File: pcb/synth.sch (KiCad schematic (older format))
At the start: 62 parts, among them J1 Conn_01x06, J2 Barrel_Jack_Switch, SW1 SW_Push, SW10 SW_Push, SW11 SW_Push, SW12 SW_Push, SW13 SW_Push, SW14 SW_Push, SW15 SW_Push, SW16 SW_Push, SW17 SW_Push, SW18 SW_Push, SW19 SW_Push, SW2 SW_Push, SW20 SW_Push, SW21 SW_Push, SW22 SW_Push, SW23 SW_Push, SW24 SW_Push, SW25 SW_Push, SW26 SW_Push, SW27 SW_Push, SW28 SW_Push, SW29 SW_Push, SW3 SW_Push, SW30 SW_Push, SW4 SW_Push, SW5 SW_Push, SW6 SW_Push, SW7 SW_Push, SW8 SW_Push, SW9 SW_Push, U1 LD1117S33TR_SOT223, U2 STM32F407VGTx, Y1 Crystal_8

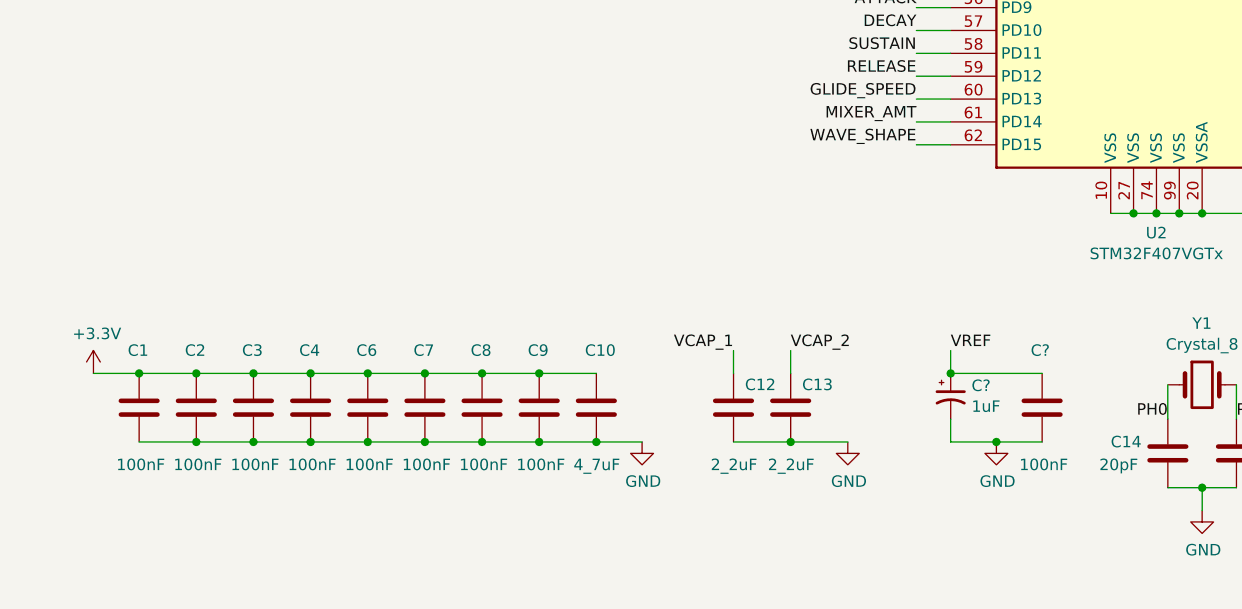
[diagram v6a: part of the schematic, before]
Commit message: Decouple VDDA similar to VREF, and connect both to VDD.
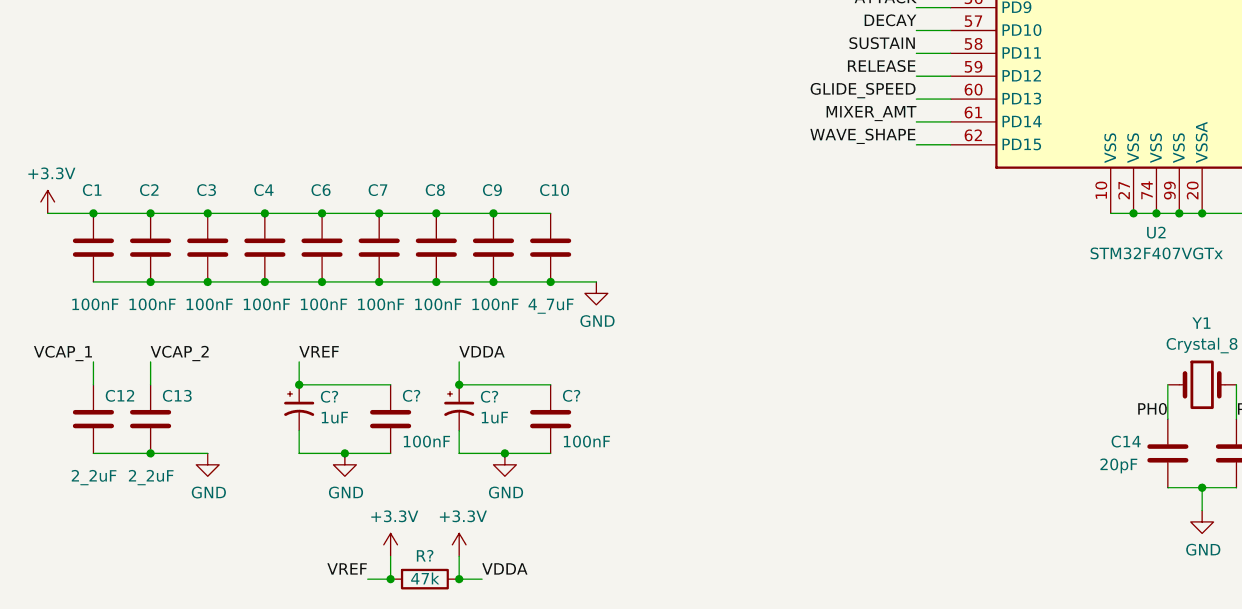
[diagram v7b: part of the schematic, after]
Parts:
- added C?: 1uF, symbol Device:CP1_Small
- added C?: 100nF, Capacitor_THT:CP_Axial_L11.0mm_D8.0mm_P15.00mm_Horizontal, symbol Device:C
- added R?: 47k, symbol Device:R
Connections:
- net VREF is gone; now on net +3V3: C?.1, C?.1, U2.21 (VREF+)
- net +3V3: now also C?.1, C?.1, R?.1, R?.2
- net GND: now also C?.2, C?.2
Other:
- moved on the sheet: C1, C10, C12, C13, C2, C3, C4, C6, C7, C8, C9, C?
